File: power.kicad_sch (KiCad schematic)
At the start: 6 parts, among them J501 power, U501 Buck

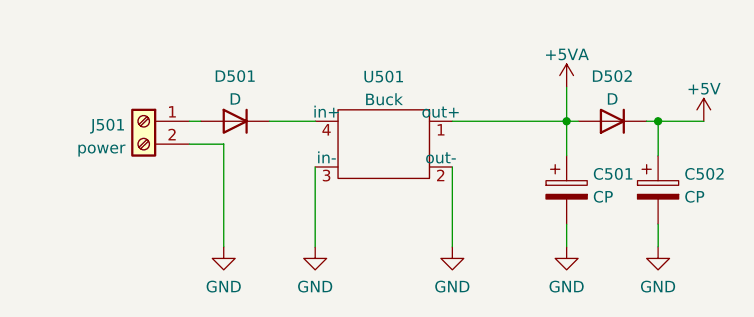
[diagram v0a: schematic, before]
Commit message: redid this project. I want to use an atmega328 so I ditched some IO. I retained 4 servo, 1 H-bridge (should make it double), 3 relays, 6 GPIO, 1 potentiometer and loconet interface. And I still have a config button
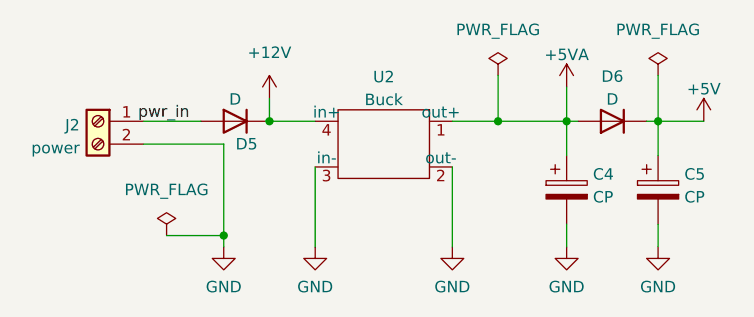
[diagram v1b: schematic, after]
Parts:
- removed C501: CP, Capacitor_THT:CP_Radial_D8.0mm_P3.50mm, symbol Device:C_Polarized
- added C4: CP, Capacitor_SMD:CP_Elec_6.3x7.7, symbol Device:C_Polarized
- C5: renamed from C502; footprint Capacitor_THT:CP_Radial_D8.0mm_P3.50mm -> Capacitor_SMD:CP_Elec_6.3x7.7; JLCPCB Part# (none) -> C125975
- renumbered D501 to D5, D502 to D6, J501 to J2, U501 to U2
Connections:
- net +5VA: now also C4.1
- net GND: now also C4.2
- net +12V: now reaches D5.1 (K), U2.4 (in+)
- net pwr_in: now reaches D5.2 (A), J2.1 (Pin_1)
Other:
- moved on the sheet: J2
